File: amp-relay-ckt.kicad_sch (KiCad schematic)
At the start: 14 parts, among them K10 HK19F-DCxxV-SHC, K11 HK19F-DCxxV-SHC, Q2 Q_PNP_BCE, Q5 BSS123, U1 LM7805_TO220

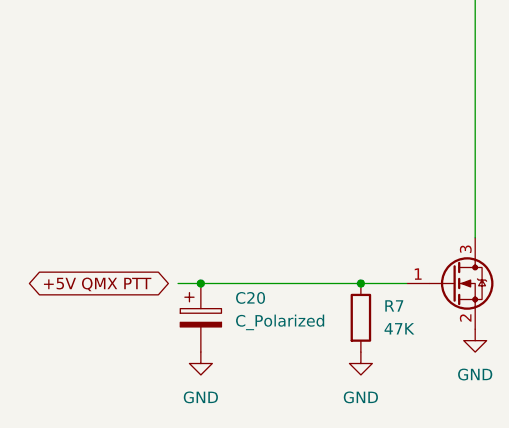
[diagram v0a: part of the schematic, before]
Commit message: all caps on LPF Chain are pF.  rest are uF
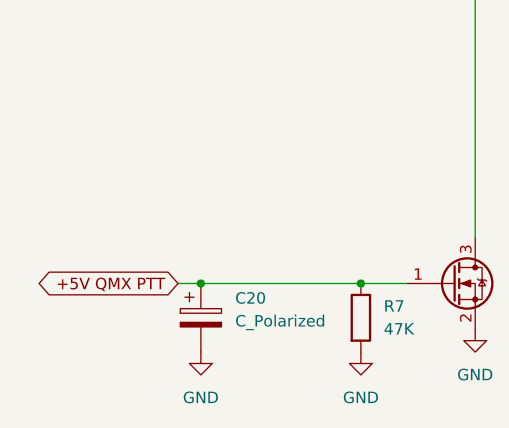
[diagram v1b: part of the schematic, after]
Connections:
- net +5V QMX PTT: now also C20.1, Q5.1 (G), R7.1
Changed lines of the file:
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@@
 	(title_block
 		(title "QMX Amp")
-		(date "2024-08-09")
-		(rev "v0.1")
+		(date "2024-08-10")
+		(rev "v0.2")
 		(company "WA7GIL")
 	)
@@
 	)
 	(junction
+		(at 102.87 101.6)
+		(diameter 0)
+		(color 0 0 0 0)
+	)
+	(junction
 		(at 87.63 74.93)
 		(diameter 0)
@@
 	)
 	(junction
-		(at 102.87 101.6)
-		(diameter 0)
-		(color 0 0 0 0)
-	)
-	(junction
 		(at 82.55 74.93)
 		(diameter 0)
@@
 	(wire
 		(pts
+			(xy 72.39 74.93) (xy 82.55 74.93)
+		)
+		(stroke
+			(width 0)
+			(type default)
+		)
+	)
+	(wire
+		(pts
+			(xy 134.62 69.85) (xy 134.62 74.93)
+		)
+		(stroke
+			(width 0)
+			(type default)
+		)
+	)
+	(wire
+		(pts
+			(xy 153.67 53.34) (xy 153.67 62.23)
+		)
+		(stroke
+			(width 0)
+			(type default)
+		)
+	)
+	(wire
+		(pts
+			(xy 82.55 74.93) (xy 83.82 74.93)
+		)
+		(stroke
+			(width 0)
+			(type default)
+		)
+	)
+	(wire
+		(pts
+			(xy 59.69 53.34) (xy 72.39 53.34)
+		)
+		(stroke
+			(width 0)
+			(type default)
+		)
+	)
+	(wire
+		(pts
+			(xy 52.07 120.65) (xy 69.85 120.65)
+		)
+		(stroke
+			(width 0)
+			(type default)
+		)
+	)
+	(wire
+		(pts
+			(xy 72.39 69.85) (xy 72.39 74.93)
+		)
+		(stroke
+			(width 0)
+			(type default)
+		)
+	)
+	(wire
+		(pts
 			(xy 102.87 101.6) (xy 116.84 101.6)
-		)
-		(stroke
-			(width 0)
-			(type default)
-		)
-	)
-	(wire
-		(pts
-			(xy 72.39 74.93) (xy 82.55 74.93)
-		)
-		(stroke
-			(width 0)
-			(type default)
-		)
-	)
-	(wire
-		(pts
-			(xy 134.62 69.85) (xy 134.62 74.93)
-		)
-		(stroke
-			(width 0)
-			(type default)
-		)
-	)
-	(wire
-		(pts
-			(xy 153.67 53.34) (xy 153.67 62.23)
-		)
-		(stroke
-			(width 0)
-			(type default)
-		)
-	)
-	(wire
-		(pts
-			(xy 82.55 74.93) (xy 83.82 74.93)
-		)
-		(stroke
-			(width 0)
-			(type default)
-		)
-	)
-	(wire
-		(pts
-			(xy 59.69 53.34) (xy 72.39 53.34)
-		)
-		(stroke
-			(width 0)
-			(type default)
-		)
-	)
-	(wire
-		(pts
-			(xy 52.07 120.65) (xy 69.85 120.65)
-		)
-		(stroke
-			(width 0)
-			(type default)
-		)
-	)
-	(wire
-		(pts
-			(xy 72.39 69.85) (xy 72.39 74.93)
 		)
 		(stroke
@@
 	(global_label "+5V QMX PTT"
 		(shape bidirectional)
-		(at 33.02 120.65 0)
+		(at 49.53 120.65 180)
 		(fields_autoplaced yes)
 		(effects
@@
 				(size 1.27 1.27)
 			)
-			(justify left)
+			(justify right)
 		)
 		(property "Intersheetrefs" "${INTERSHEET_REFS}"
-			(at 50.1186 120.65 0)
-			(effects
-				(font
-					(size 1.27 1.27)
-				)
-				(justify left)
+			(at 32.4314 120.65 0)
+			(effects
+				(font
+					(size 1.27 1.27)
+				)
+				(justify right)
 				(hide yes)
 			)
@@
 		)
 		(instances
-			(project ""
+			(project "QMX-amp"
 				(path "/e63e39d7-6ac0-4ffd-8aa3-1841a4541b55/6e8a5723-6162-4126-acdf-190058cf1f27"
 					(reference "#PWR027")
@@
 		)
 		(instances
-			(project ""
+			(project "QMX-amp"
 				(path "/e63e39d7-6ac0-4ffd-8aa3-1841a4541b55/6e8a5723-6162-4126-acdf-190058cf1f27"
 					(reference "Q5")

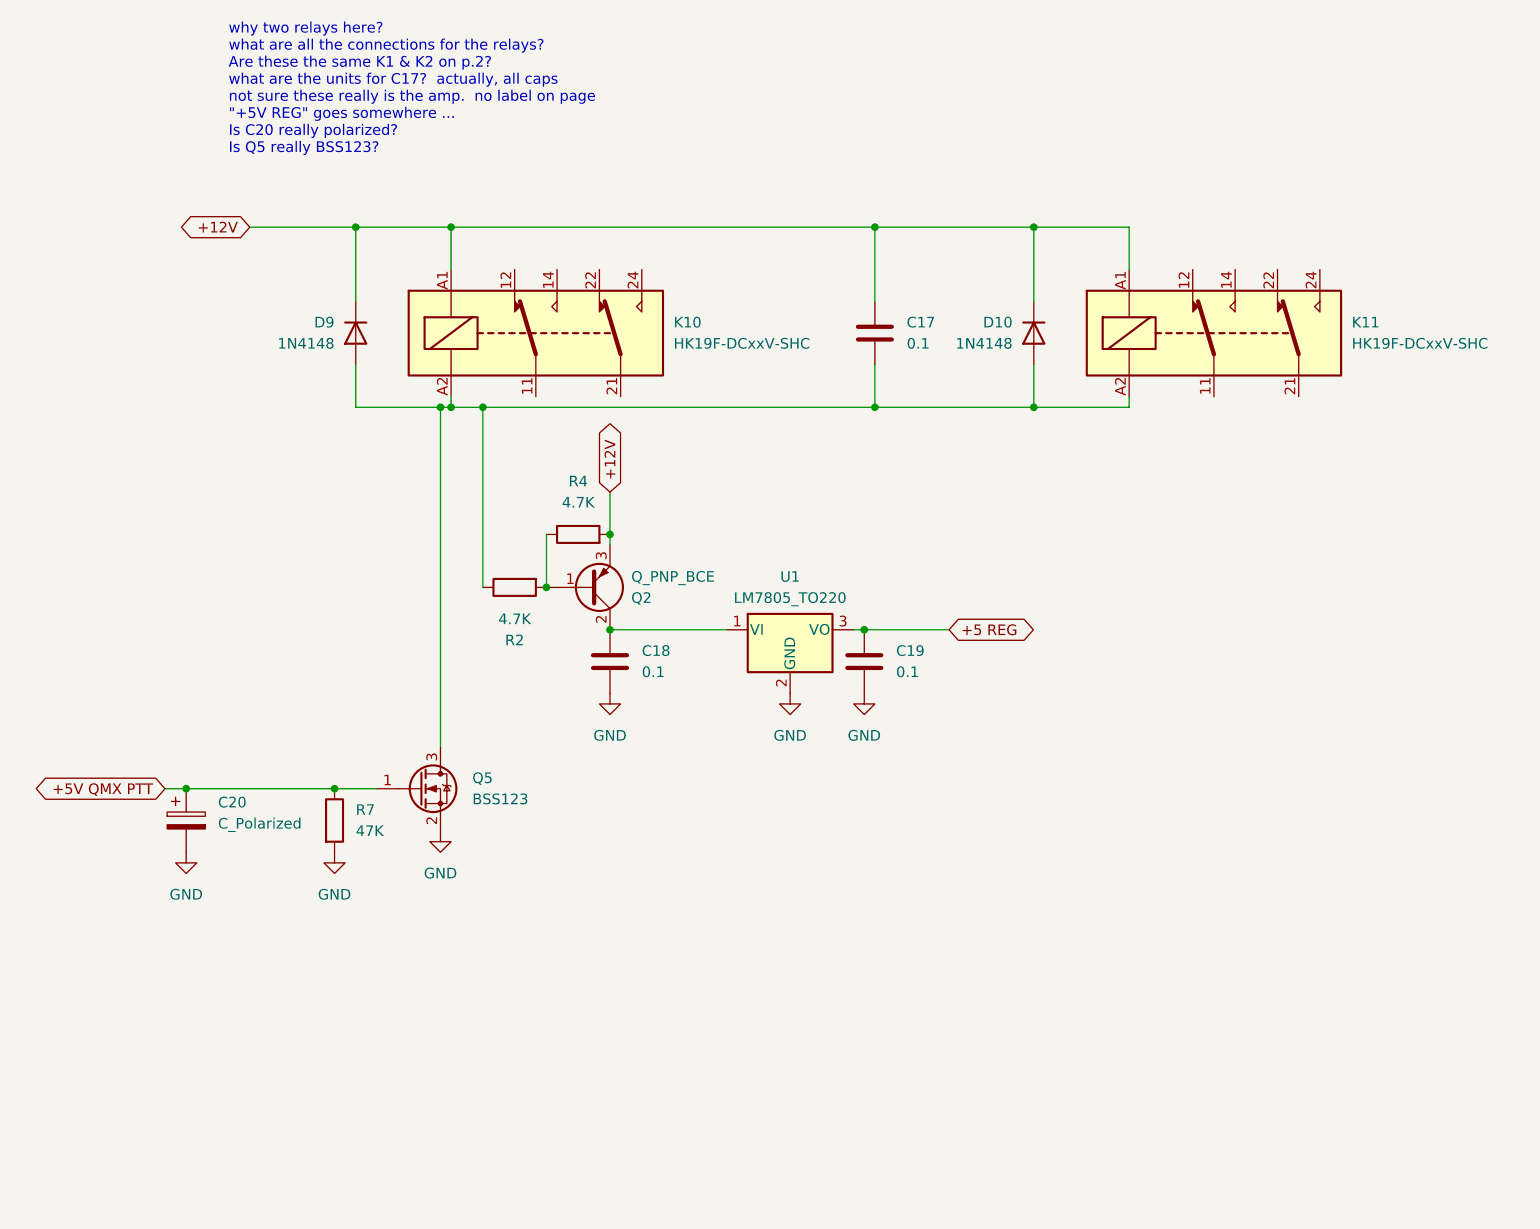
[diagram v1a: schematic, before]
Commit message: I think all the caps have units now
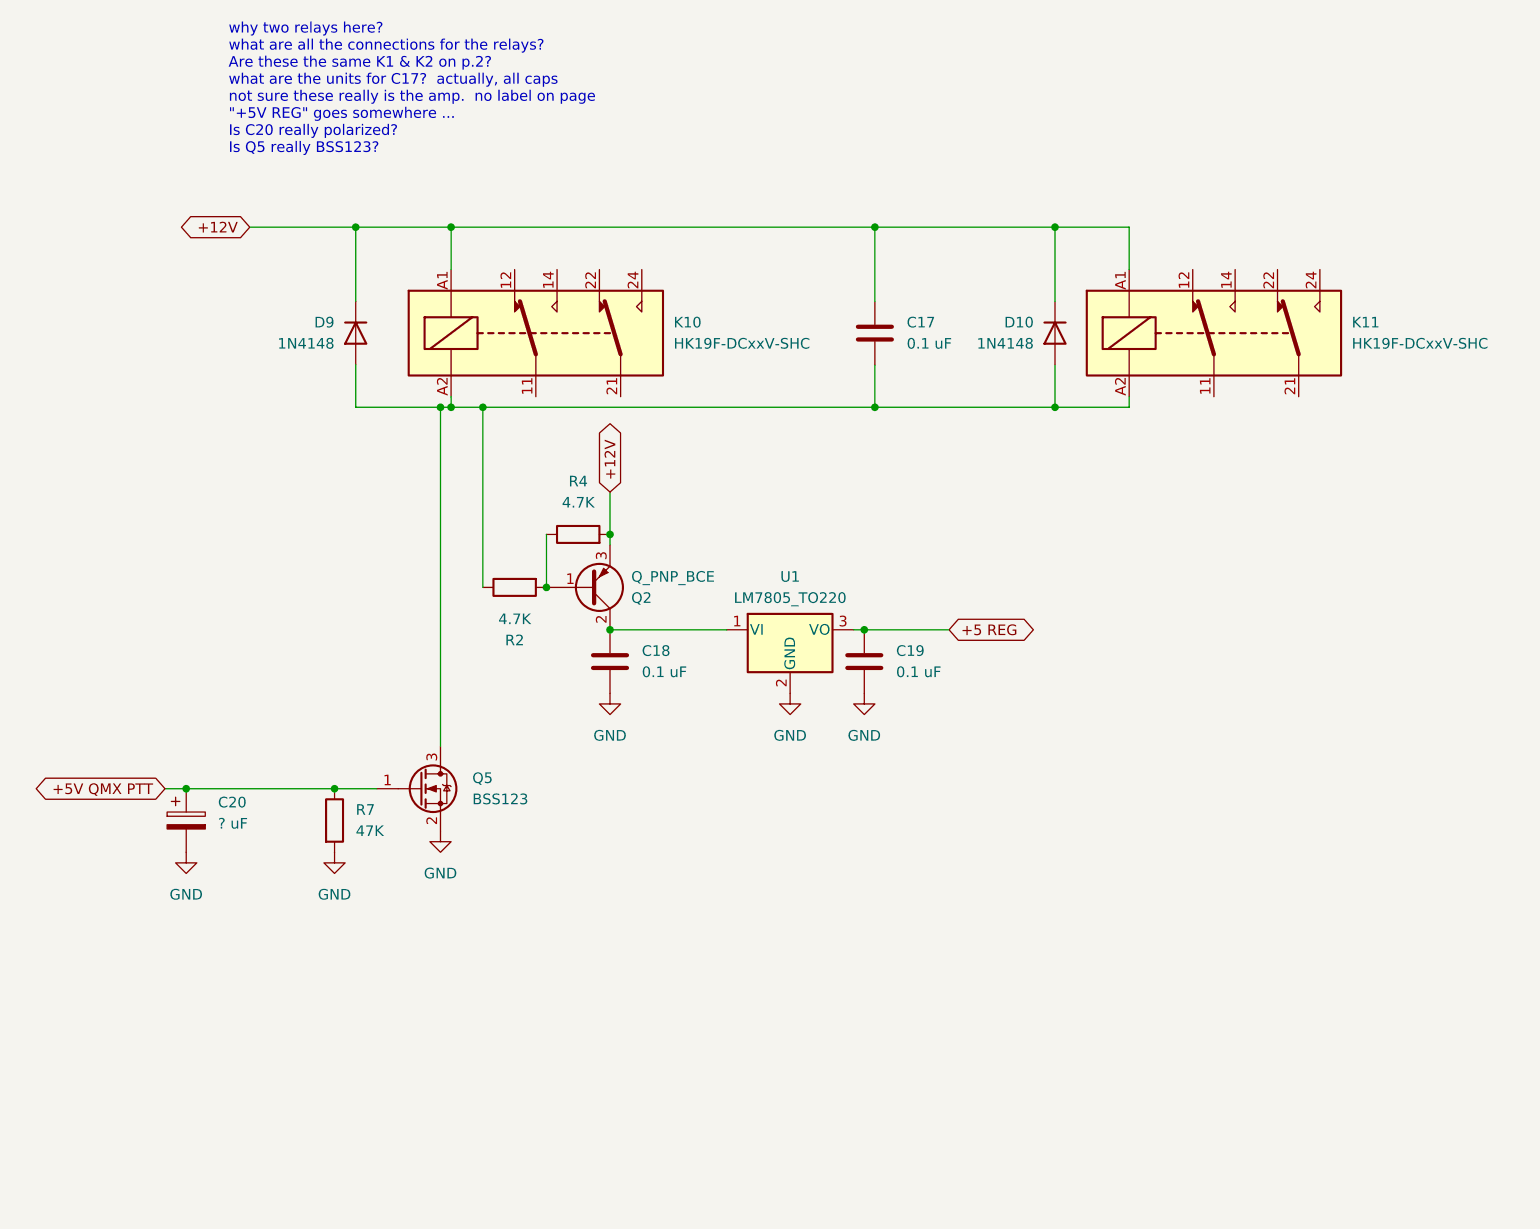
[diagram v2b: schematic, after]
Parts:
- C17, C18, C19: value 0.1 -> 0.1 uF
- C20: value C_Polarized -> ? uF
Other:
- moved on the sheet: D10
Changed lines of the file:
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@@
+	)
+	(junction
+		(at 156.21 53.34)
+		(diameter 0)
+		(color 0 0 0 0)
 	)
 	(junction
@@
 	)
 	(junction
-		(at 153.67 74.93)
-		(diameter 0)
-		(color 0 0 0 0)
-	)
-	(junction
-		(at 153.67 53.34)
+		(at 156.21 74.93)
 		(diameter 0)
 		(color 0 0 0 0)
@@
 	(wire
 		(pts
-			(xy 153.67 53.34) (xy 153.67 62.23)
+			(xy 156.21 53.34) (xy 156.21 62.23)
 		)
 		(stroke
@@
 	(wire
 		(pts
-			(xy 153.67 69.85) (xy 153.67 74.93)
+			(xy 156.21 69.85) (xy 156.21 74.93)
 		)
 		(stroke
@@
 	(wire
 		(pts
-			(xy 134.62 53.34) (xy 153.67 53.34)
-		)
-		(stroke
-			(width 0)
-			(type default)
-		)
-	)
-	(wire
-		(pts
-			(xy 153.67 53.34) (xy 165.1 53.34)
+			(xy 134.62 53.34) (xy 156.21 53.34)
 		)
 		(stroke
@@
 	(wire
 		(pts
-			(xy 165.1 74.93) (xy 153.67 74.93)
+			(xy 165.1 74.93) (xy 156.21 74.93)
 		)
 		(stroke
@@
 	(wire
 		(pts
-			(xy 153.67 74.93) (xy 134.62 74.93)
+			(xy 134.62 74.93) (xy 156.21 74.93)
 		)
 		(stroke
@@
 		(pts
 			(xy 83.82 53.34) (xy 134.62 53.34)
+		)
+		(stroke
+			(width 0)
+			(type default)
+		)
+	)
+	(wire
+		(pts
+			(xy 156.21 53.34) (xy 165.1 53.34)
 		)
 		(stroke
@@
 			)
 		)
-		(property "Value" "0.1"
+		(property "Value" "0.1 uF"
 			(at 106.68 106.6799 0)
 			(effects
@@
 	(symbol
 		(lib_id "Device:D")
-		(at 153.67 66.04 90)
+		(at 156.21 66.04 90)
 		(mirror x)
 		(unit 1)
@@
 		(dnp no)
 		(property "Reference" "D10"
-			(at 151.13 64.7699 90)
+			(at 153.67 64.7699 90)
 			(effects
 				(font
@@
 		)
 		(property "Value" "1N4148"
-			(at 151.13 67.3099 90)
+			(at 153.67 67.3099 90)
 			(effects
 				(font
@@
 		)
 		(property "Footprint" ""
-			(at 153.67 66.04 0)
+			(at 156.21 66.04 0)
 			(effects
 				(font
@@
 		)
 		(property "Datasheet" "1N4148"
-			(at 153.67 66.04 0)
+			(at 156.21 66.04 0)
 			(effects
 				(font
@@
 		)
 		(property "Description" "Diode"
-			(at 153.67 66.04 0)
+			(at 156.21 66.04 0)
 			(effects
 				(font
@@
 		)
 		(property "Sim.Device" "D"
-			(at 153.67 66.04 0)
+			(at 156.21 66.04 0)
 			(effects
 				(font
@@
 		)
 		(property "Sim.Pins" "1=K 2=A"
-			(at 153.67 66.04 0)
+			(at 156.21 66.04 0)
 			(effects
 				(font
@@
 			)
 		)
-		(property "Value" "C_Polarized"
+		(property "Value" "? uF"
 			(at 55.88 124.8409 0)
 			(effects
@@
 			)
 		)
-		(property "Value" "0.1"
+		(property "Value" "0.1 uF"
 			(at 137.16 106.6799 0)
 			(effects
@@
 			)
 		)
-		(property "Value" "0.1"
+		(property "Value" "0.1 uF"
 			(at 138.43 67.3099 0)
 			(effects

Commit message: does NOT pass ERC.  Something going on with LM7805
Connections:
- net +5 REG renamed +5V REG
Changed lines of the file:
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@@
 		)
 	)
-	(global_label "+5 REG"
+	(global_label "+5V REG"
 		(shape bidirectional)
 		(at 143.51 101.6 0)
@@
 		)
 		(property "Intersheetrefs" "${INTERSHEET_REFS}"
-			(at 155.0448 101.6 0)
+			(at 156.1334 101.6 0)
 			(effects
 				(font

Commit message: trying to get K1 & K2 appear in multiple places, yet be recognized as identical.  Currently reporting dup K1
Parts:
- renumbered K10 to K1
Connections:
- no-connect marks 0 -> 3
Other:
- note added: "+5V REG connects to bias pots. What is a 'bias pot' and where is it in the schematic?"
- note added: "Are these the same K1 & K2 on p.2? YES How can I make K1 & K2 appear two different places yet be identical?"
- note removed: "why two relays here? what are all the connections for the relays? Are these the same K1 & K2 on p.2? what are the units for C17? actually, all caps not sure these really is the amp. no label on page "+5V REG" goes somewhere ... Is C20 really polarized? Is Q5 really BSS123?"
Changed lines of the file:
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@@
 		(color 0 0 0 0)
 	)
+	(no_connect
+		(at 101.6 58.42)
+	)
+	(no_connect
+		(at 106.68 58.42)
+	)
+	(no_connect
+		(at 104.14 73.66)
+	)
 	(wire
 		(pts
@@
 		)
 	)
-	(text "why two relays here?\nwhat are all the connections for the relays?\nAre these the same K1 & K2 on p.2?\nwhat are the units for C17?  actually, all caps\nnot sure these really is the amp.  no label on page\n\"+5V REG\" goes somewhere ...\nIs C20 really polarized?\nIs Q5 really BSS123?"
+	(text "Are these the same K1 & K2 on p.2?  YES\nHow can I make K1 & K2 appear two different places\nyet be identical?"
 		(exclude_from_sim no)
 		(at 57.15 36.83 0)
@@
 			)
 			(justify left)
+		)
+	)
+	(text "+5V REG connects to bias pots.\nWhat is a 'bias pot' and where is it in the schematic?"
+		(exclude_from_sim no)
+		(at 177.038 107.188 0)
+		(effects
+			(font
+				(size 1.27 1.27)
+			)
 		)
 	)
@@
 		(dnp no)
 		(fields_autoplaced yes)
-		(property "Reference" "K10"
+		(property "Reference" "K1"
 			(at 110.49 64.7699 0)
 			(effects
@@
 			(project "QMX-amp"
 				(path "/e63e39d7-6ac0-4ffd-8aa3-1841a4541b55/6e8a5723-6162-4126-acdf-190058cf1f27"
-					(reference "K10")
+					(reference "K1")
 					(unit 1)
 				)

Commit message: checkpoint progress from 240810
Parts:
- added C99: C_Polarized, symbol Device:C_Polarized
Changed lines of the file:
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@@
+	)
+	(symbol
+		(lib_id "Device:C_Polarized")
+		(at 59.69 167.64 0)
+		(unit 1)
+		(exclude_from_sim no)
+		(in_bom yes)
+		(on_board yes)
+		(dnp no)
+		(fields_autoplaced yes)
+		(property "Reference" "C99"
+			(at 63.5 165.4809 0)
+			(effects
+				(font
+					(size 1.27 1.27)
+				)
+				(justify left)
+			)
+		)
+		(property "Value" "C_Polarized"
+			(at 63.5 168.0209 0)
+			(effects
+				(font
+					(size 1.27 1.27)
+				)
+				(justify left)
+			)
+		)
+		(property "Footprint" ""
+			(at 60.6552 171.45 0)
+			(effects
+				(font
+					(size 1.27 1.27)
+				)
+				(hide yes)
+			)
+		)
+		(property "Datasheet" "~"
+			(at 59.69 167.64 0)
+			(effects
+				(font
+					(size 1.27 1.27)
+				)
+				(hide yes)
+			)
+		)
+		(property "Description" "Polarized capacitor"
+			(at 59.69 167.64 0)
+			(effects
+				(font
+					(size 1.27 1.27)
+				)
+				(hide yes)
+			)
+		)
+		(pin "2"
+		)
+		(pin "1"
+		)
+		(instances
+			(project ""
+				(path "/e63e39d7-6ac0-4ffd-8aa3-1841a4541b55/6e8a5723-6162-4126-acdf-190058cf1f27"
+					(reference "C99")
+					(unit 1)
+				)
+			)
+		)
 	)
 	(symbol
